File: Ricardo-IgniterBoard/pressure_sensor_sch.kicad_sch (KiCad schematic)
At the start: 17 parts, among them IC5 ADS131M04IRUKR, J5 1053131104

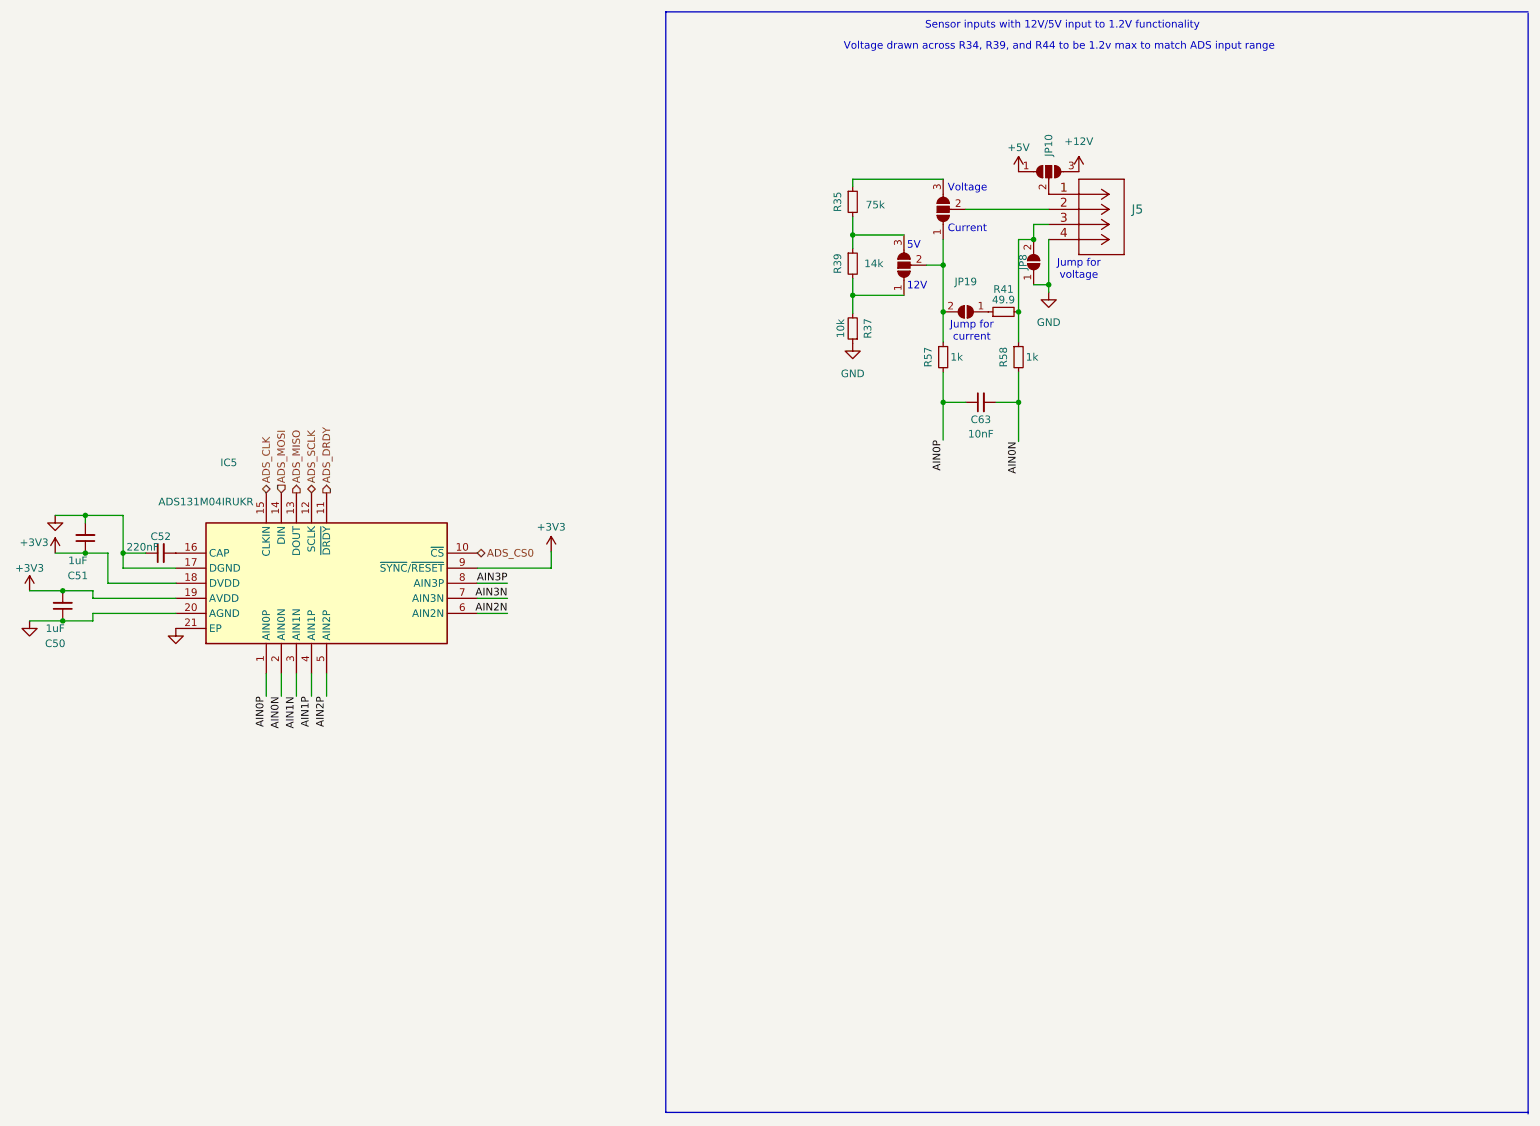
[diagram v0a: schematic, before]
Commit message: Adjusting numbers and adding hieratical pins
Adjusted number of pyro and PT modules and connected everything to the root
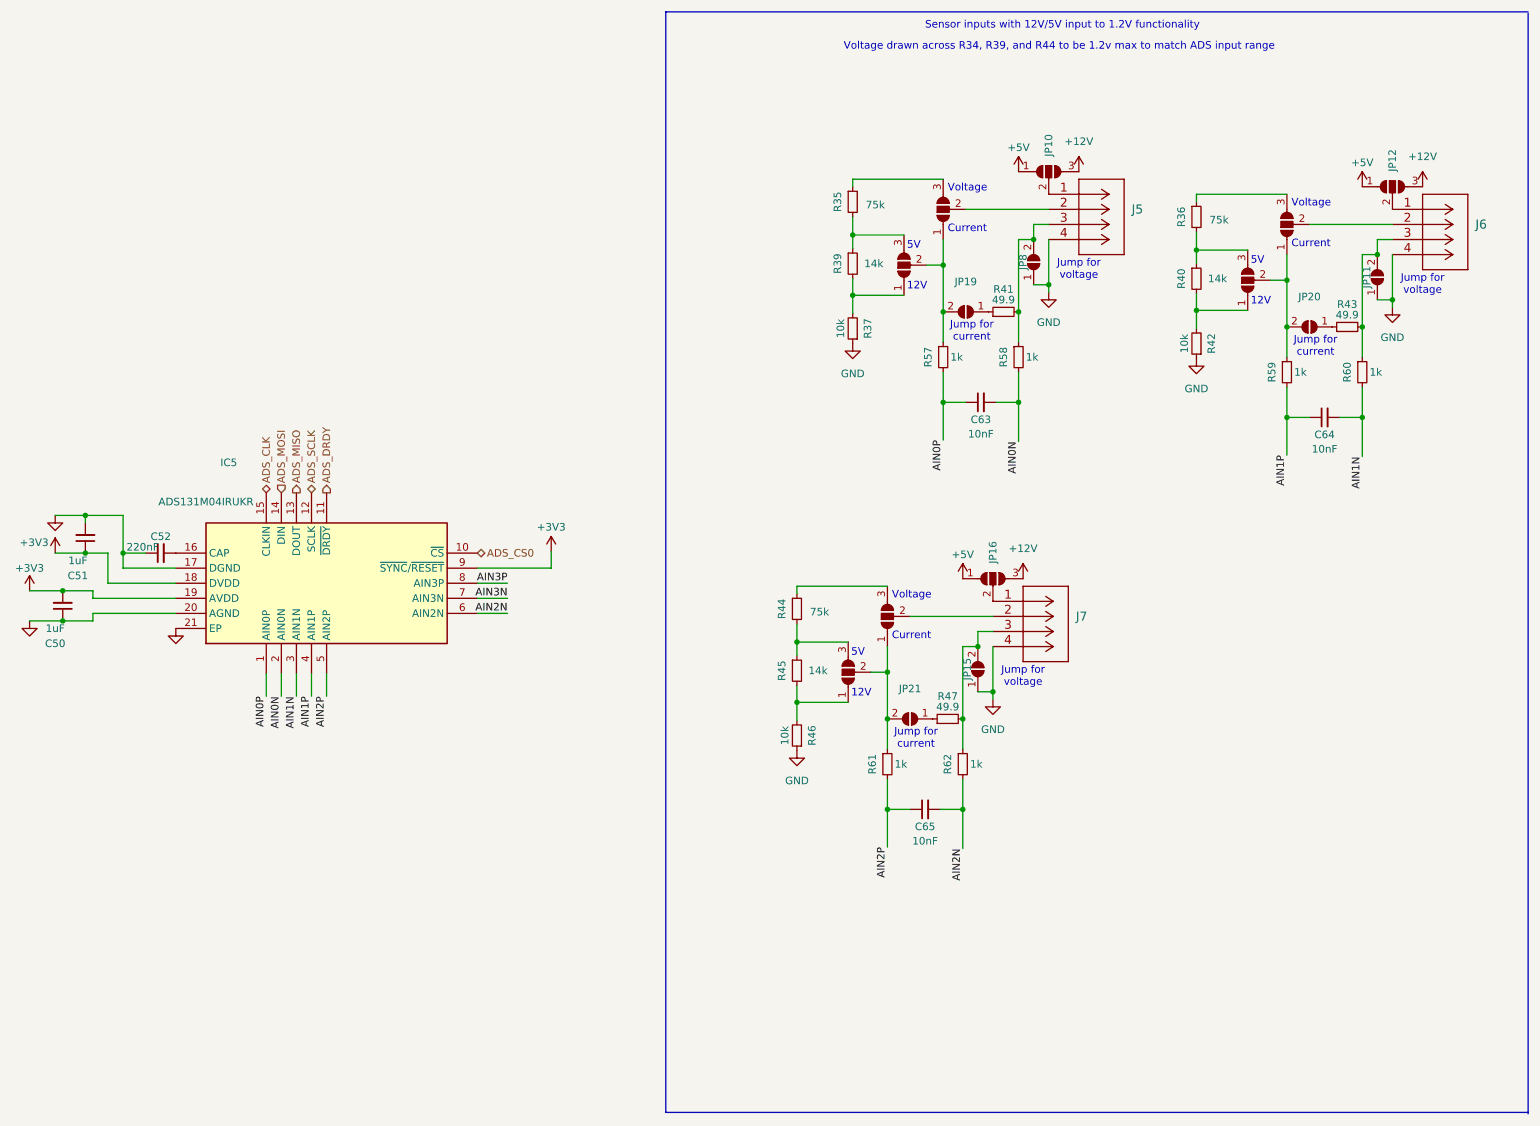
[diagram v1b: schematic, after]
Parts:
- added C64, C65: 10nF, Capacitor_SMD:C_0402_1005Metric, symbol Device:C_Small
- added J6, J7: 1053131104, Connector_Molex:Molex_Nano-Fit_105313-xx04_1x04_P2.50mm_Horizontal, symbol iclr:1053131104
- added JP11, JP15, JP20, JP21: SolderJumper_2_Open, iclr:SmallerSolderJP, symbol Jumper:SolderJumper_2_Open
- added JP12, JP13, JP14, JP16, JP7, JP9: SolderJumper_3_Open, Jumper:SolderJumper-3_P1.3mm_Open_RoundedPad1.0x1.5mm_NumberLabels, symbol Jumper:SolderJumper_3_Open
- added R36, R44: 75k, Resistor_SMD:R_0402_1005Metric, symbol Device:R_Small
- added R40, R45: 14k, Resistor_SMD:R_0402_1005Metric, symbol Device:R_Small
- added R42, R46: 10k, Resistor_SMD:R_0402_1005Metric, symbol Device:R_Small
- added R43, R47: 49.9, Resistor_SMD:R_0402_1005Metric, symbol Device:R_Small
- added R59, R60, R61, R62: 1k, Resistor_SMD:R_0402_1005Metric, symbol Device:R_Small
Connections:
- net +12V: now also JP12.3 (B), JP16.3 (B)
- net +5V: now also JP12.1 (A), JP16.1 (A)
- net AIN1N: now also C64.2, R60.2
- net AIN1P: now also C64.1, R59.2
- net AIN2N: now also C65.2, R62.2
- net AIN2P: now also C65.1, R61.2
- net GND: now also J6.4, J7.4, JP11.1 (A), JP15.1 (A), R42.1, R46.1
- new net: JP20.2 (B), JP7.2 (C), JP9.1 (A), R59.1
- new net: J6.2, JP9.2 (C)
- new net: JP9.3 (B), R36.1
- new net: JP20.1 (A), R43.1
- new net: J6.3, JP11.2 (B), R43.2, R60.1
- new net: JP7.1 (A), R40.2, R42.2
- new net: JP7.3 (B), R36.2, R40.1
- new net: JP21.1 (A), R47.1
- new net: JP13.2 (C), JP14.1 (A), JP21.2 (B), R61.1
- new net: J7.1, JP16.2 (C)
- new net: J7.2, JP14.2 (C)
- new net: J7.3, JP15.2 (B), R47.2, R62.1
- new net: J6.1, JP12.2 (C)
- new net: JP13.3 (B), R44.2, R45.1
- new net: JP13.1 (A), R45.2, R46.2
- new net: JP14.3 (B), R44.1

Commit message: Assigning components
And added the thermocouple
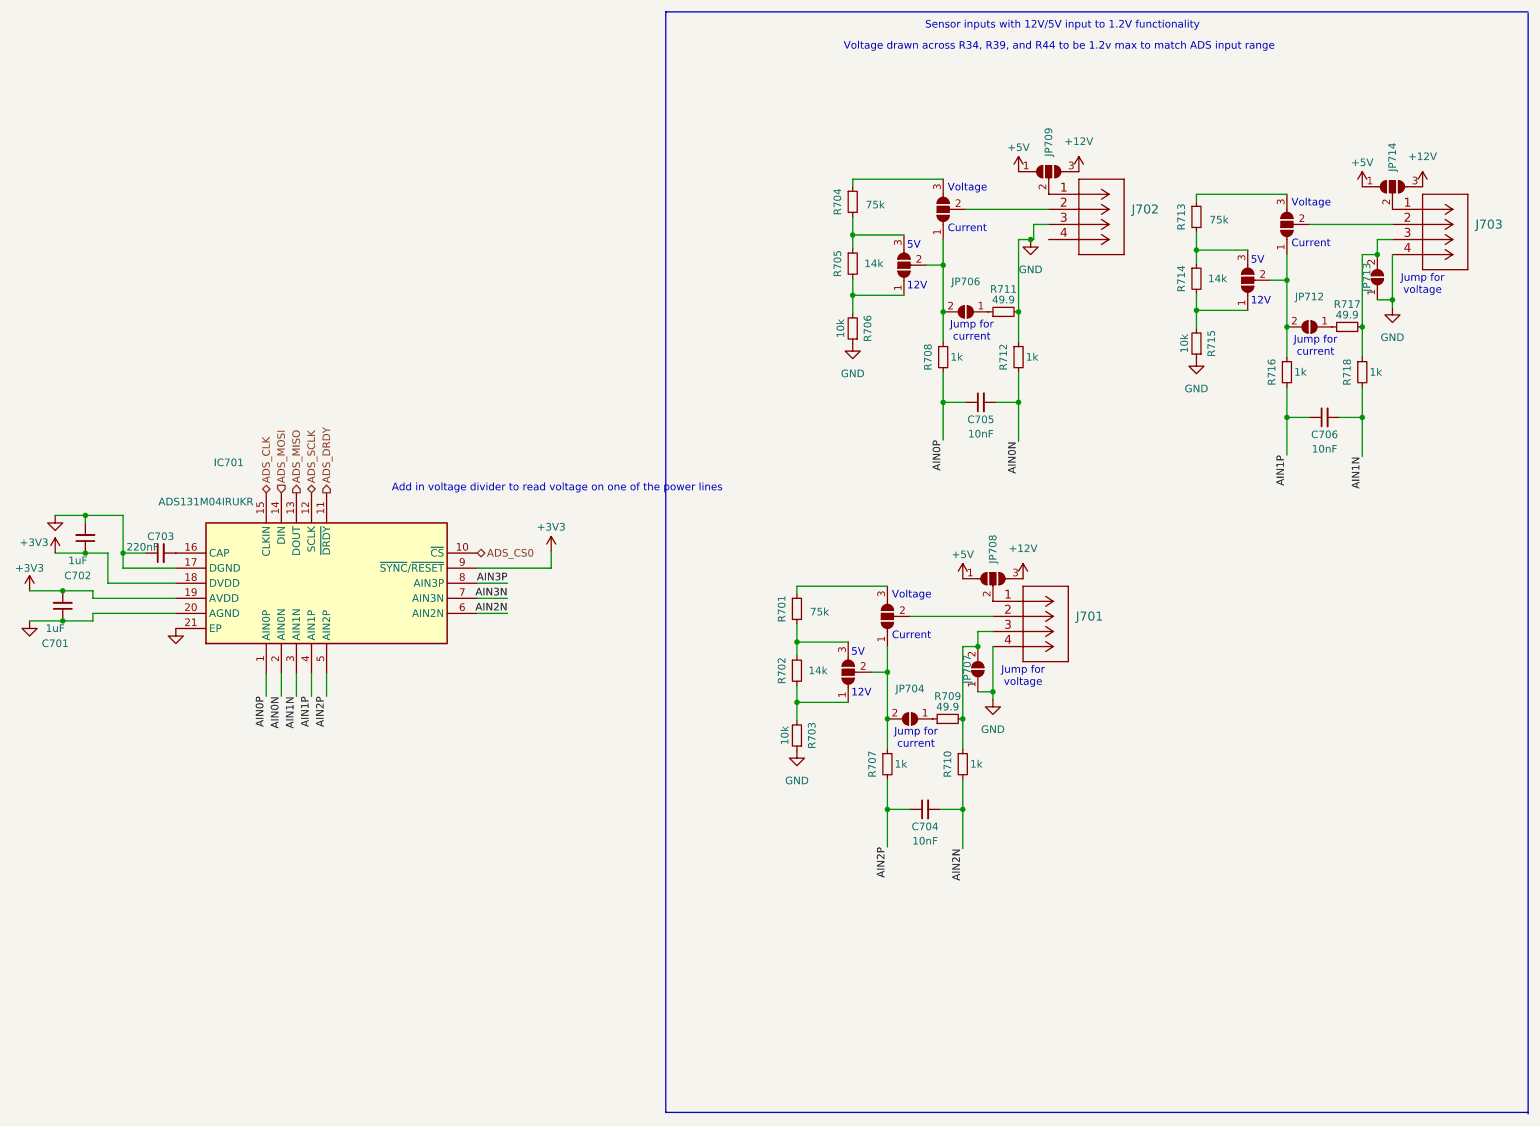
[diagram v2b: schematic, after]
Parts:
- removed JP8: SolderJumper_2_Open, iclr:SmallerSolderJP, symbol Jumper:SolderJumper_2_Open
- IC701: renamed from IC5; footprint QFN40P300X300X80-21N-D -> (none)
- renumbered C50 to C701, C51 to C702, C52 to C703, C65 to C704, C63 to C705, C64 to C706, J7 to J701, J5 to J702, J6 to J703, JP13 to JP701, JP14 to JP702, JP6 to JP703, JP21 to JP704, JP5 to JP705, JP19 to JP706, JP15 to JP707, JP16 to JP708, JP10 to JP709, JP7 to JP710, JP9 to JP711, JP20 to JP712, JP11 to JP713, JP12 to JP714, R44 to R701, R45 to R702, R46 to R703, R35 to R704, R39 to R705, R37 to R706, R61 to R707, R57 to R708, R47 to R709, R62 to R710, R41 to R711, R58 to R712, R36 to R713, R40 to R714, R42 to R715, R59 to R716, R43 to R717, R60 to R718
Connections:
- net GND: now also J702.3, R711.2, R712.1; no longer J702.4
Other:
- note added: "Add in voltage divider to read voltage on one of the power lines"

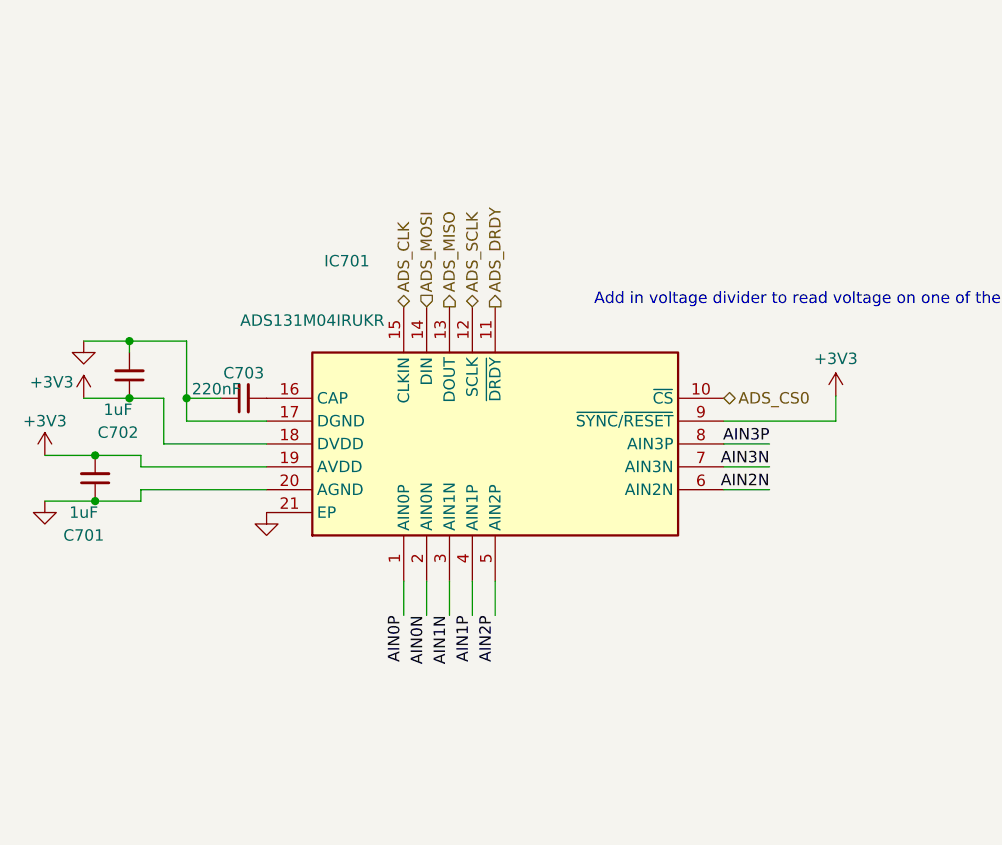
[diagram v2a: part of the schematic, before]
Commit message: some more changes
added current sensor for solenoid, fixed optocouplers
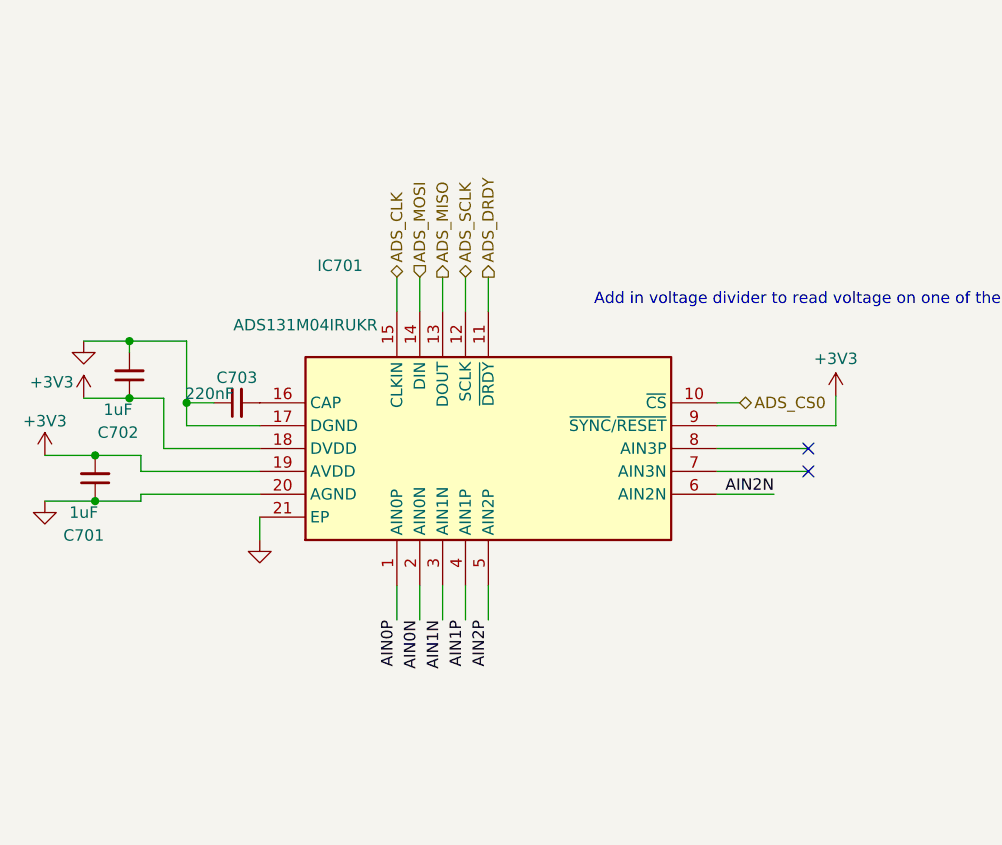
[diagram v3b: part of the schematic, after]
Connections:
- net AIN3N: no longer names the net of IC701.7 (AIN3N)
- net AIN3P: no longer names the net of IC701.8 (AIN3P)
- no-connect marks 0 -> 2
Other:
- moved on the sheet: C703, IC701

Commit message: Assigning footprints
and adding them to layout
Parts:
- IC701: footprint (none) -> iclr:ADS131M04IRUKR
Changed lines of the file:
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@@
 			)
 		)
-		(property "Footprint" ""
+		(property "Footprint" "iclr:ADS131M04IRUKR"
 			(at 158.42 97.79 0)
 			(effects
